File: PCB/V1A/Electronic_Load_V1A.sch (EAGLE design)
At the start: 209 parts, among them IC101 LM50, IC102 LM50, IC301 7805T, IC302 OPA77P, Q101 SIRC10DP, Q102 SIRC10DP, Q103 BC817-16SMD, Q104 BC817-16SMD, Q105 BC807-16SMD, Q106 SIRC10DP, Q107 IXTK102N65X2R+, Q108 SIRC10DP, Q109 SIRC10DP, Q110 SIRC10DP, Q111 IXTK102N65X2R+, Q601 BC807-16SMD, Q602 BC807-16SMD, Q603 BC807-16SMD, Q604 BC807-16SMD, Q605 BC807-16SMD, Q606 BC807-16SMD, Q607 BC807-16SMD, Q608 BC807-16SMD, Q609 BC807-16SMD, Q610 BC807-16SMD, Q611 BC807-16SMD, Q612 BC807-16SMD, U101 AD420, U102 AD420, U103 LTC1865L, U104 LT1014I, U201 AD620, U202 AD620, U203 AD620, U204 AD620, U205 AD620, U206 LTC1865L, U207 LTC1865L, U208 LTC1865L, U301 MAX743, U601 HCPL-063N, U602 HCPL-063N, U603 HCPL-063N, U604 HCPL-063N, U605 HCPL-063N, U606 HCPL-063N

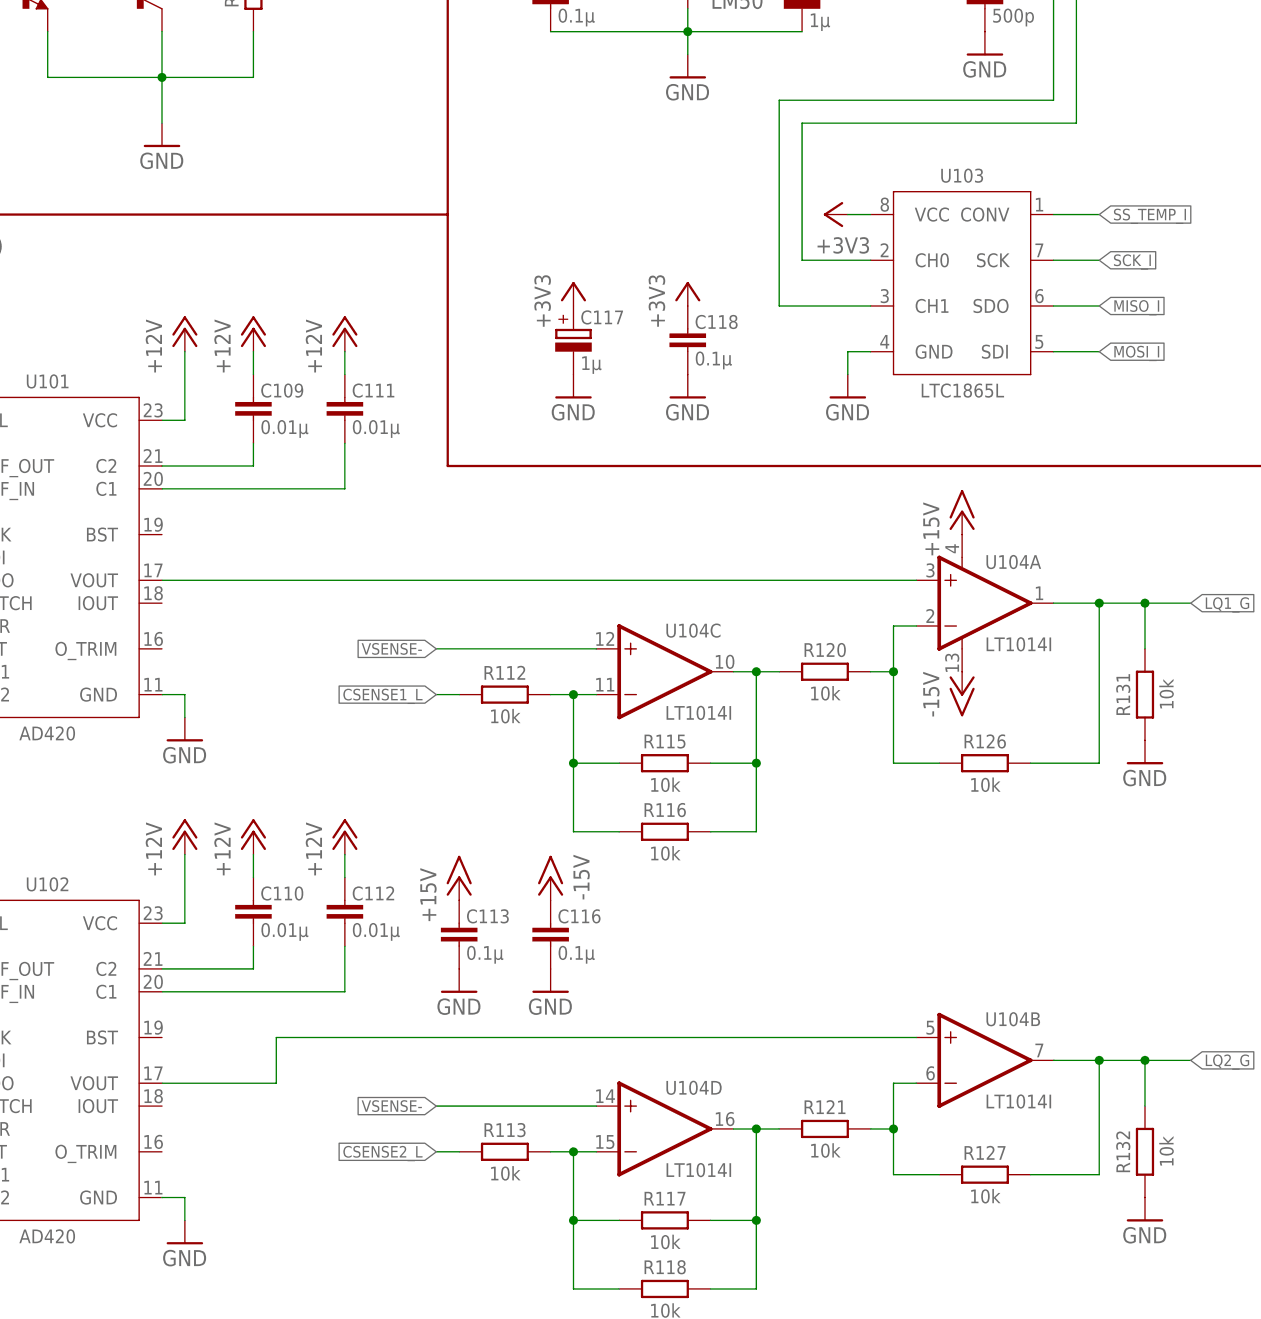
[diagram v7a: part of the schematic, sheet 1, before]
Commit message: Added heatsink models, ADC/DAC layout
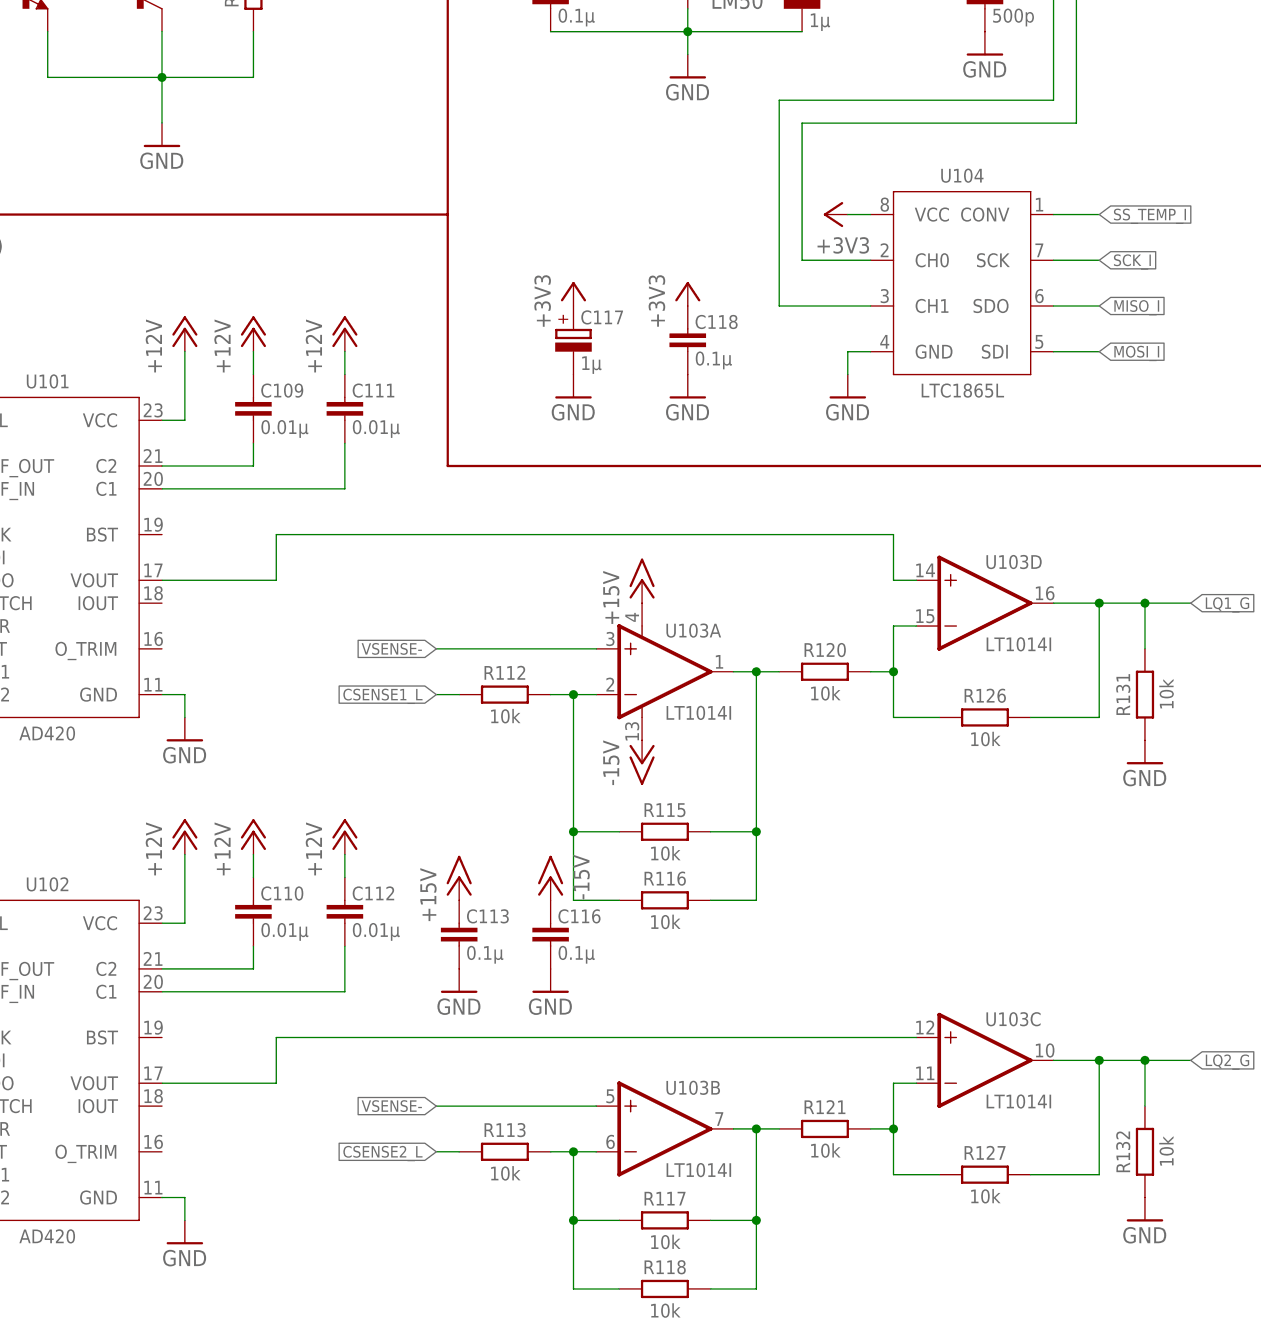
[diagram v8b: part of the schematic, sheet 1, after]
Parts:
- U103: value LTC1865L -> LT1014I; device ic:LTC1865L -> ic:LT1014ISW
- U104: value LT1014I -> LTC1865L; device ic:LT1014ISW -> ic:LTC1865L
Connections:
- removed net BYP_G_ISO: C610.1, R610.1, U601.VO2
- removed net CSENSE_H1: U201.+, U203.-
- removed net CSENSE_H2: U202.+, U204.-
- removed net CSENSE_L1: U203.+
- removed net CSENSE_L2: U204.+
- removed net DAC_CLR: Q603.B
- removed net DAC_FAULT_ISO: Q605.B
- removed net SS_DAC_ISO: C607.1, R607.1, U601.VO1
- net +15V: now also U103A.V+; no longer U104A.V+
- net +3V3: now also U104.VCC; no longer U103.VCC
- net -15V: now also U103A.V-; no longer U104A.V-
- net BYP_I: now also C610.1, R610.1, U601.VO2
- net CLR_DAC_I: now also Q603.B
- net CSENSE1_H: now also U201.+, U203.-
- net CSENSE1_L: now also U203.+
- net CSENSE2_H: now also U202.+, U204.-
- net CSENSE2_L: now also U204.+
- net FLT_DAC_I: now also Q605.B
- net GND: now also U104.GND; no longer U103.GND
- net LQ1_G: now also U103D.OUT; no longer U104A.OUT
- net LQ2_G: now also U103C.OUT; no longer U104B.OUT
- net MISO_I: now also U104.SDO; no longer U103.SDO
- net MOSI_I: now also U104.SDI; no longer U103.SDI
- net N$10: now also U103D.+IN; no longer U104A.+IN
- net N$11: now also U103C.+IN; no longer U104B.+IN
- net N$12: now also U103D.-IN; no longer U104A.-IN
- net N$13: now also U103A.OUT; no longer U104C.OUT
- net N$14: now also U103A.-IN; no longer U104C.-IN
- net N$15: now also U103B.-IN; no longer U104D.-IN
- net N$16: now also U103B.OUT; no longer U104D.OUT
- net N$9: now also U103C.-IN; no longer U104B.-IN
- net SCK_I: now also U104.SCK; no longer U103.SCK
- net SS_CH: now also Q610.B; no longer Q607.B
- net SS_CH_I: now also C623.1, R623.1, U605.VO2; no longer C620.1, R620.1, U605.VO1
- net SS_CL: now also Q607.B; no longer Q610.B
- net SS_CL_I: now also C620.1, R620.1, U605.VO1; no longer C623.1, R623.1, U605.VO2
- net SS_DAC_I: now also C607.1, R607.1, U601.VO1
- net SS_TEMP: now also Q608.B; no longer Q611.B
- net SS_TEMP_I: now also C621.1, R621.1, U104.CONV, U606.VO1; no longer C624.1, R624.1, U103.CONV, U606.VO2
- net SS_V: now also Q611.B; no longer Q608.B
- net SS_V_I: now also C624.1, R624.1, U606.VO2; no longer C621.1, R621.1, U606.VO1
- net TEMP1: now also U104.CH0; no longer U103.CH0
- net TEMP2: now also U104.CH1; no longer U103.CH1
- net VSENSE-: now also U103A.+IN, U103B.+IN; no longer U104C.+IN, U104D.+IN
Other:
- moved on the sheet: R115, R116, R126
